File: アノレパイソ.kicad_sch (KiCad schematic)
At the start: 29 parts, among them SW1 RotaryEncoder_Switch, SW2 SW_PUSH, SW3 SW_PUSH, SW5 SW_PUSH, SW6 SW_PUSH, SW7 SW_PUSH, SW8 SW_PUSH, SW9 SW_PUSH, U1 Micon_BLEMicroPro

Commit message: Add files via upload
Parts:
- LED1, LED10, LED11, LED12, LED2, LED3, LED4, LED5, LED6, LED7, LED8, LED9: footprint kbd:YS-SK6812MINI-E -> LED_SMD:LED_SK6812MINI_PLCC4_3.5x3.5mm_P1.75mm
- SW1: footprint (none) -> Rotary_Encoder:RotaryEncoder_Alps_EC12E-Switch_Vertical_H20mm
- SW2, SW3, SW5, SW6, SW7, SW8, SW9: footprint (none) -> Button_Switch_Keyboard:SW_Cherry_MX_1.00u_PCB
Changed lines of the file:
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@@
 			)
 		)
-		(property "Footprint" "kbd:YS-SK6812MINI-E"
+		(property "Footprint" "LED_SMD:LED_SK6812MINI_PLCC4_3.5x3.5mm_P1.75mm"
 			(at 313.69 152.4 0)
 			(effects
@@
 			)
 		)
-		(property "Footprint" ""
+		(property "Footprint" "Button_Switch_Keyboard:SW_Cherry_MX_1.00u_PCB"
 			(at 248.92 66.04 0)
 			(effects
@@
 			)
 		)
-		(property "Footprint" "kbd:YS-SK6812MINI-E"
+		(property "Footprint" "LED_SMD:LED_SK6812MINI_PLCC4_3.5x3.5mm_P1.75mm"
 			(at 212.09 152.4 0)
 			(effects
@@
 			)
 		)
-		(property "Footprint" "kbd:YS-SK6812MINI-E"
+		(property "Footprint" "LED_SMD:LED_SK6812MINI_PLCC4_3.5x3.5mm_P1.75mm"
 			(at 34.29 152.4 0)
 			(effects
@@
 			)
 		)
-		(property "Footprint" ""
+		(property "Footprint" "Rotary_Encoder:RotaryEncoder_Alps_EC12E-Switch_Vertical_H20mm"
 			(at 143.764 34.29 0)
 			(effects
@@
 			)
 		)
-		(property "Footprint" "kbd:YS-SK6812MINI-E"
+		(property "Footprint" "LED_SMD:LED_SK6812MINI_PLCC4_3.5x3.5mm_P1.75mm"
 			(at 237.49 152.4 0)
 			(effects
@@
 			)
 		)
-		(property "Footprint" "kbd:YS-SK6812MINI-E"
+		(property "Footprint" "LED_SMD:LED_SK6812MINI_PLCC4_3.5x3.5mm_P1.75mm"
 			(at 262.89 152.4 0)
 			(effects
@@
 			)
 		)
-		(property "Footprint" ""
+		(property "Footprint" "Button_Switch_Keyboard:SW_Cherry_MX_1.00u_PCB"
 			(at 172.72 66.04 0)
 			(effects
@@
 			)
 		)
-		(property "Footprint" "kbd:YS-SK6812MINI-E"
+		(property "Footprint" "LED_SMD:LED_SK6812MINI_PLCC4_3.5x3.5mm_P1.75mm"
 			(at 186.69 152.4 0)
 			(effects
@@
 			)
 		)
-		(property "Footprint" "kbd:YS-SK6812MINI-E"
+		(property "Footprint" "LED_SMD:LED_SK6812MINI_PLCC4_3.5x3.5mm_P1.75mm"
 			(at 288.29 152.4 0)
 			(effects
@@
 			)
 		)
-		(property "Footprint" "kbd:YS-SK6812MINI-E"
+		(property "Footprint" "LED_SMD:LED_SK6812MINI_PLCC4_3.5x3.5mm_P1.75mm"
 			(at 135.89 152.4 0)
 			(effects
@@
 			)
 		)
-		(property "Footprint" ""
+		(property "Footprint" "Button_Switch_Keyboard:SW_Cherry_MX_1.00u_PCB"
 			(at 48.26 77.47 0)
 			(effects
@@
 			)
 		)
-		(property "Footprint" ""
+		(property "Footprint" "Button_Switch_Keyboard:SW_Cherry_MX_1.00u_PCB"
 			(at 210.82 66.04 0)
 			(effects
@@
 			)
 		)
-		(property "Footprint" "kbd:YS-SK6812MINI-E"
+		(property "Footprint" "LED_SMD:LED_SK6812MINI_PLCC4_3.5x3.5mm_P1.75mm"
 			(at 110.49 152.4 0)
 			(effects
@@
 			)
 		)
-		(property "Footprint" ""
+		(property "Footprint" "Button_Switch_Keyboard:SW_Cherry_MX_1.00u_PCB"
 			(at 172.72 82.55 0)
 			(effects
@@
 			)
 		)
-		(property "Footprint" ""
+		(property "Footprint" "Button_Switch_Keyboard:SW_Cherry_MX_1.00u_PCB"
 			(at 248.92 85.09 0)
 			(effects
@@
 			)
 		)
-		(property "Footprint" "kbd:YS-SK6812MINI-E"
+		(property "Footprint" "LED_SMD:LED_SK6812MINI_PLCC4_3.5x3.5mm_P1.75mm"
 			(at 85.09 152.4 0)
 			(effects
@@
 			)
 		)
-		(property "Footprint" "kbd:YS-SK6812MINI-E"
+		(property "Footprint" "LED_SMD:LED_SK6812MINI_PLCC4_3.5x3.5mm_P1.75mm"
 			(at 59.69 152.4 0)
 			(effects
@@
 			)
 		)
-		(property "Footprint" ""
+		(property "Footprint" "Button_Switch_Keyboard:SW_Cherry_MX_1.00u_PCB"
 			(at 210.82 83.82 0)
 			(effects
@@
 			)
 		)
-		(property "Footprint" "kbd:YS-SK6812MINI-E"
+		(property "Footprint" "LED_SMD:LED_SK6812MINI_PLCC4_3.5x3.5mm_P1.75mm"
 			(at 161.29 152.4 0)
 			(effects

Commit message: PCBエディタで可能な限り部品の配置と配線を実施
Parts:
- U2: value ~ -> SO1602AWWB-UC-WB-U; footprint (none) -> AKI-SO1602AWGB:SO1602AWWB-UC-WB-U
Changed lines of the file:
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@@
 			)
 		)
-		(property "Value" "~"
+		(property "Value" "SO1602AWWB-UC-WB-U"
 			(at 105.41 54.61 0)
 			(effects
@@
 			)
 		)
-		(property "Footprint" ""
+		(property "Footprint" "AKI-SO1602AWGB:SO1602AWWB-UC-WB-U"
 			(at 109.22 71.12 0)
 			(effects

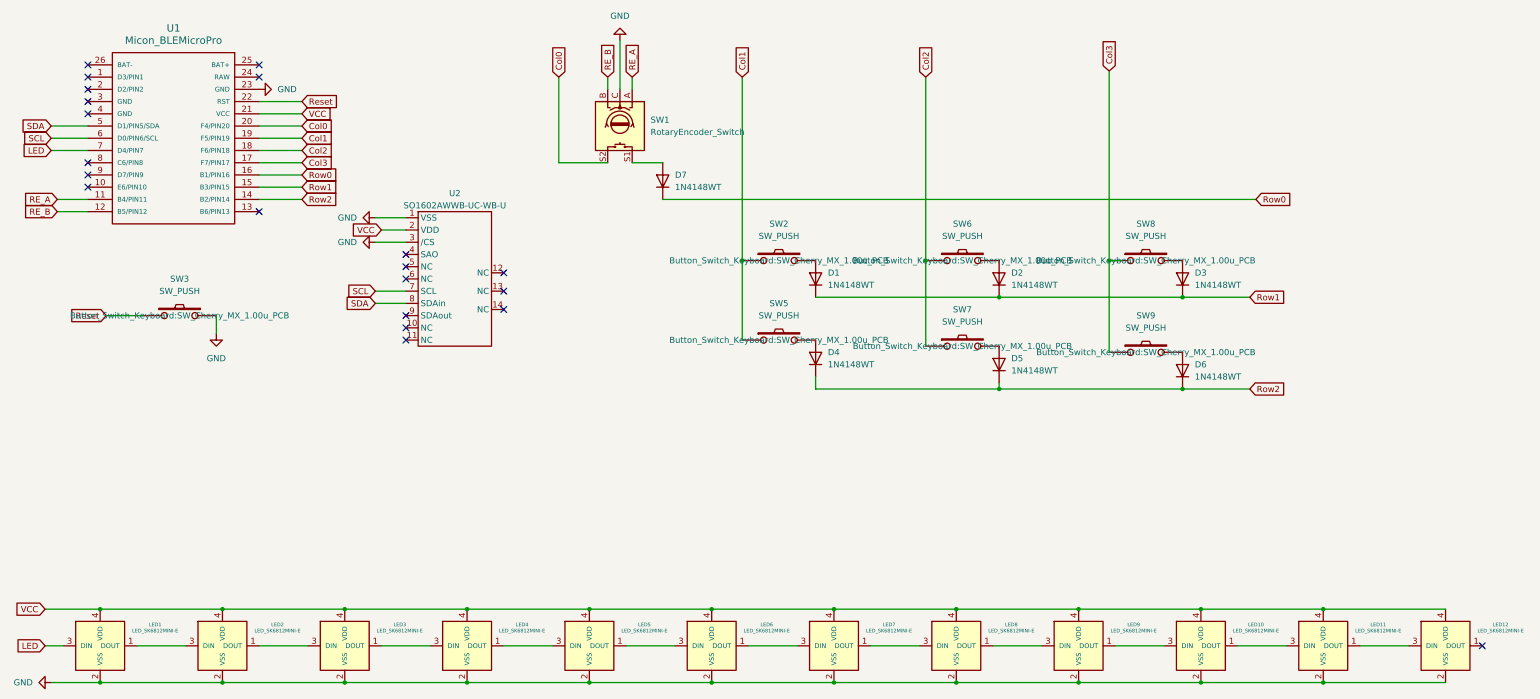
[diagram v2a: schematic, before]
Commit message: μCOMを残して配線完了。
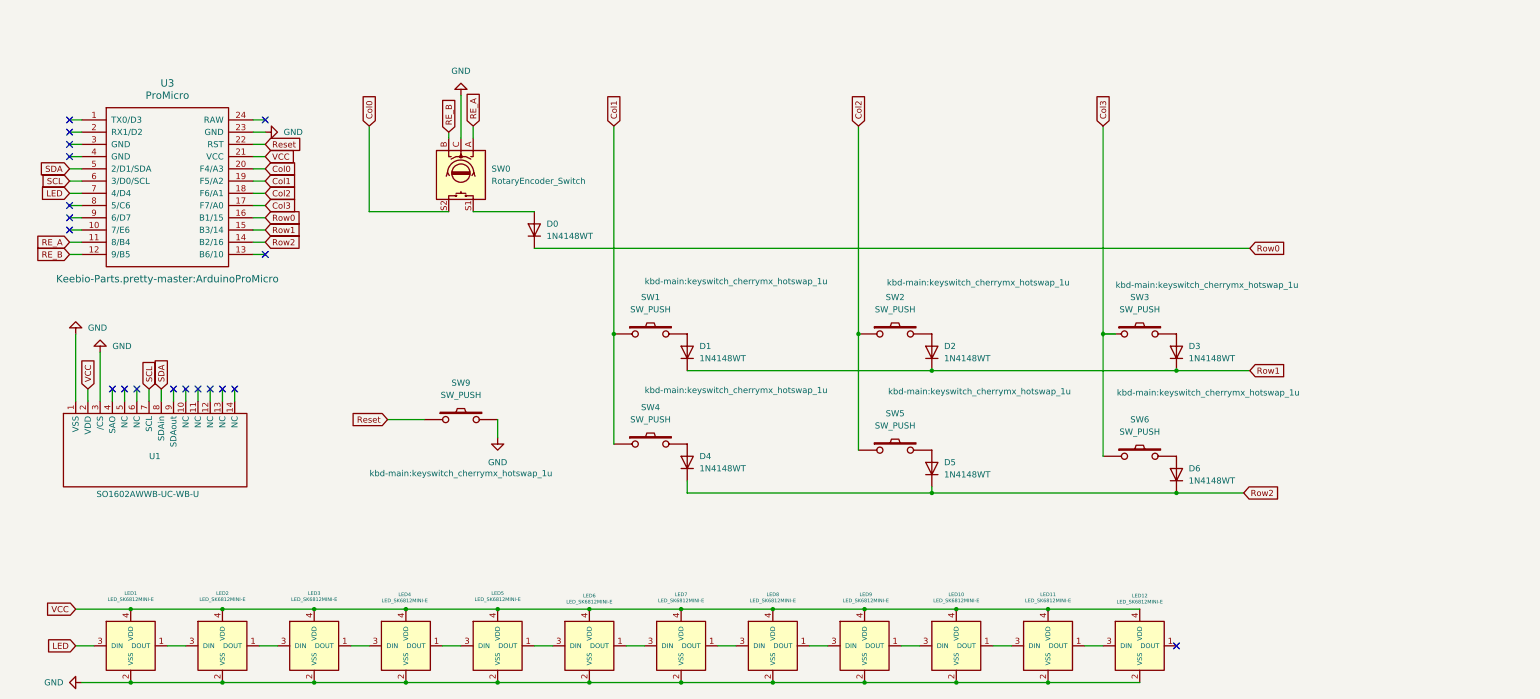
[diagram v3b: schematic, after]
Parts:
- removed U1: Micon_BLEMicroPro, symbol Salicylic_kbd:Micon_BLEMicroPro
- removed U2: SO1602AWWB-UC-WB-U, AKI-SO1602AWGB:SO1602AWWB-UC-WB-U, symbol kbd:SO1602AWWB-UC-WB-U
- added U1: SO1602AWWB-UC-WB-U, AKI-SO1602AWGB:SO1602AWWB-UC-WB-U, symbol kbd:SO1602AWWB-UC-WB-U
- added U3: ProMicro, Keebio-Parts.pretty-master:ArduinoProMicro, symbol kbd:ProMicro
- SW1: renamed from SW2; footprint Button_Switch_Keyboard:SW_Cherry_MX_1.00u_PCB -> kbd-main:keyswitch_cherrymx_hotswap_1u
- SW2: renamed from SW6; footprint Button_Switch_Keyboard:SW_Cherry_MX_1.00u_PCB -> kbd-main:keyswitch_cherrymx_hotswap_1u
- SW3: renamed from SW8; footprint Button_Switch_Keyboard:SW_Cherry_MX_1.00u_PCB -> kbd-main:keyswitch_cherrymx_hotswap_1u
- SW4: renamed from SW5; footprint Button_Switch_Keyboard:SW_Cherry_MX_1.00u_PCB -> kbd-main:keyswitch_cherrymx_hotswap_1u
- SW5: renamed from SW7; footprint Button_Switch_Keyboard:SW_Cherry_MX_1.00u_PCB -> kbd-main:keyswitch_cherrymx_hotswap_1u
- SW6: renamed from SW9; footprint Button_Switch_Keyboard:SW_Cherry_MX_1.00u_PCB -> kbd-main:keyswitch_cherrymx_hotswap_1u
- SW9: renamed from SW3; footprint Button_Switch_Keyboard:SW_Cherry_MX_1.00u_PCB -> kbd-main:keyswitch_cherrymx_hotswap_1u
- renumbered D7 to D0, SW1 to SW0
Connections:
- net Col0: now also U3.20 (F4/A3)
- net Col1: now also U3.19 (F5/A2)
- net Col2: now also U3.18 (F6/A1)
- net Col3: now also U3.17 (F7/A0)
- net GND: now also U1.1 (VSS), U1.3 (/CS), U3.23 (GND)
- net LED: now also U3.7 (4/D4)
- net RE_A: now also U3.11 (8/B4)
- net RE_B: now also U3.12 (9/B5)
- net Reset: now also U3.22 (RST)
- net Row0: now also U3.16 (B1/15)
- net Row1: now also U3.15 (B3/14)
- net Row2: now also U3.14 (B2/16)
- net SCL: now also U1.7 (SCL), U3.6 (3/D0/SCL)
- net SDA: now also U1.8 (SDAin), U3.5 (2/D1/SDA)
- net VCC: now also U1.2 (VDD), U3.21 (VCC)
- no-connect marks 21 -> 19
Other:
- moved on the sheet: D0, D1, D2, D3, D4, D5, D6, LED1, LED10, LED11, LED12, LED3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

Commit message: いったん今の知識でやれることは全部終わり。赤ペン待ち。
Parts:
- SW9: footprint kbd-main:keyswitch_cherrymx_hotswap_1u -> kbd-main:ResetSW
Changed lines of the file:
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@@
 			)
 		)
-		(property "Footprint" "kbd-main:keyswitch_cherrymx_hotswap_1u"
+		(property "Footprint" "kbd-main:ResetSW"
 			(at 106.68 110.236 0)
 			(effects

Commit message: 電気系のエラーはすべてなくした。
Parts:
- LED1, LED10, LED11, LED12, LED2, LED3, LED4, LED5, LED6, LED7, LED8, LED9: footprint LED_SMD:LED_SK6812MINI_PLCC4_3.5x3.5mm_P1.75mm -> kbd-main:YS-SK6812MINI-E
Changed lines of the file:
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@@
 			)
 		)
-		(property "Footprint" "LED_SMD:LED_SK6812MINI_PLCC4_3.5x3.5mm_P1.75mm"
+		(property "Footprint" "kbd-main:YS-SK6812MINI-E"
 			(at 250.19 152.4 0)
 			(effects
@@
 			)
 		)
-		(property "Footprint" "LED_SMD:LED_SK6812MINI_PLCC4_3.5x3.5mm_P1.75mm"
+		(property "Footprint" "kbd-main:YS-SK6812MINI-E"
 			(at 173.99 152.4 0)
 			(effects
@@
 			)
 		)
-		(property "Footprint" "LED_SMD:LED_SK6812MINI_PLCC4_3.5x3.5mm_P1.75mm"
+		(property "Footprint" "kbd-main:YS-SK6812MINI-E"
 			(at 40.64 152.4 0)
 			(effects
@@
 			)
 		)
-		(property "Footprint" "LED_SMD:LED_SK6812MINI_PLCC4_3.5x3.5mm_P1.75mm"
+		(property "Footprint" "kbd-main:YS-SK6812MINI-E"
 			(at 193.04 152.4 0)
 			(effects
@@
 			)
 		)
-		(property "Footprint" "LED_SMD:LED_SK6812MINI_PLCC4_3.5x3.5mm_P1.75mm"
+		(property "Footprint" "kbd-main:YS-SK6812MINI-E"
 			(at 212.09 152.4 0)
 			(effects
@@
 			)
 		)
-		(property "Footprint" "LED_SMD:LED_SK6812MINI_PLCC4_3.5x3.5mm_P1.75mm"
+		(property "Footprint" "kbd-main:YS-SK6812MINI-E"
 			(at 154.94 152.4 0)
 			(effects
@@
 			)
 		)
-		(property "Footprint" "LED_SMD:LED_SK6812MINI_PLCC4_3.5x3.5mm_P1.75mm"
+		(property "Footprint" "kbd-main:YS-SK6812MINI-E"
 			(at 231.14 152.4 0)
 			(effects
@@
 			)
 		)
-		(property "Footprint" "LED_SMD:LED_SK6812MINI_PLCC4_3.5x3.5mm_P1.75mm"
+		(property "Footprint" "kbd-main:YS-SK6812MINI-E"
 			(at 116.84 152.4 0)
 			(effects
@@
 			)
 		)
-		(property "Footprint" "LED_SMD:LED_SK6812MINI_PLCC4_3.5x3.5mm_P1.75mm"
+		(property "Footprint" "kbd-main:YS-SK6812MINI-E"
 			(at 97.79 152.4 0)
 			(effects
@@
 			)
 		)
-		(property "Footprint" "LED_SMD:LED_SK6812MINI_PLCC4_3.5x3.5mm_P1.75mm"
+		(property "Footprint" "kbd-main:YS-SK6812MINI-E"
 			(at 78.74 152.4 0)
 			(effects
@@
 			)
 		)
-		(property "Footprint" "LED_SMD:LED_SK6812MINI_PLCC4_3.5x3.5mm_P1.75mm"
+		(property "Footprint" "kbd-main:YS-SK6812MINI-E"
 			(at 59.69 152.4 0)
 			(effects
@@
 			)
 		)
-		(property "Footprint" "LED_SMD:LED_SK6812MINI_PLCC4_3.5x3.5mm_P1.75mm"
+		(property "Footprint" "kbd-main:YS-SK6812MINI-E"
 			(at 135.89 152.4 0)
 			(effects

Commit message: 2/5(水)定例MTG指摘対策版
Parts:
- SW0: footprint Rotary_Encoder:RotaryEncoder_Alps_EC12E-Switch_Vertical_H20mm -> z:EC12D1524406
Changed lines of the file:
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@@
 			)
 		)
-		(property "Footprint" "Rotary_Encoder:RotaryEncoder_Alps_EC12E-Switch_Vertical_H20mm"
+		(property "Footprint" "z:EC12D1524406"
 			(at 110.744 44.45 0)
 			(effects
